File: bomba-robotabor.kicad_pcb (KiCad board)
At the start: 2 copper layers, 93 parts, among them U1 74HC03, U2 74HCT08, U3 L4904

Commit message: sfd,j
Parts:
- removed the REF** at (138.4, 59.7)
- removed the REF** at (194.3, 78.7)
- removed the REF** at (191.8, 76.2)
- removed the REF** at (194.3, 76.2)
- removed the REF** at (191.8, 73.7)
- removed the REF** at (194.3, 73.7)
- removed the REF** at (191.8, 71.1)
- removed the REF** at (194.3, 71.1)
- removed the REF** at (191.8, 68.6)
- removed the REF** at (194.3, 68.6)
- removed the REF** at (191.8, 66.0)
- removed the REF** at (138.4, 57.1)
- removed the REF** at (194.3, 66.0)
- removed the REF** at (191.8, 63.5)
- removed the REF** at (194.3, 63.5)
- removed the REF** at (191.8, 61.0)
- removed the REF** at (194.3, 61.0)
- removed the REF** at (191.8, 58.4)
- removed the REF** at (194.3, 58.4)
- removed the REF** at (191.8, 55.9)
- removed the REF** at (194.3, 55.9)
- removed the REF** at (191.8, 53.3)
- removed the REF** at (163.8, 67.3)
- removed the REF** at (194.3, 53.3)
- removed the REF** at (191.8, 50.8)
- removed the REF** at (194.3, 50.8)
- removed the REF** at (191.8, 48.3)
- removed the REF** at (194.3, 48.3)
- removed the REF** at (181.6, 61.0)
- removed the REF** at (181.6, 57.1)
- removed the REF** at (166.4, 61.0)
- removed the REF** at (166.4, 57.1)
- removed the REF** at (181.6, 77.5)
- removed the REF** at (163.8, 64.8)
- removed the REF** at (166.4, 77.5)
- removed the REF** at (156.2, 77.5)
- removed the REF** at (141.0, 77.5)
- removed the REF** at (130.8, 77.5)
- removed the REF** at (115.6, 77.5)
- removed the REF** at (179.1, 72.4)
- removed the REF** at (179.1, 69.8)
- removed the REF** at (179.1, 67.3)
- removed the REF** at (179.1, 64.8)
- removed the REF** at (166.4, 69.8)
- removed the REF** at (191.8, 83.8)
- removed the REF** at (166.4, 67.3)
- removed the REF** at (166.4, 64.8)
- removed the REF** at (153.7, 57.1)
- removed the REF** at (153.7, 59.7)
- removed the REF** at (153.7, 62.2)
- removed the REF** at (153.7, 64.8)
- removed the REF** at (153.7, 67.3)
- removed the REF** at (153.7, 69.8)
- removed the REF** at (141.0, 72.4)
- removed the REF** at (141.0, 69.8)
- removed the REF** at (194.3, 83.8)
- removed the REF** at (141.0, 67.3)
- removed the REF** at (141.0, 64.8)
- removed the REF** at (141.0, 62.2)
- removed the REF** at (141.0, 59.7)
- removed the REF** at (141.0, 57.1)
- removed the REF** at (167.6, 52.1)
- removed the REF** at (152.4, 52.1)
- removed the REF** at (129.5, 57.1)
- removed the REF** at (129.5, 59.7)
- removed the REF** at (129.5, 64.8)
- removed the REF** at (191.8, 81.3)
- removed the REF** at (116.8, 69.8)
- removed the REF** at (162.6, 82.5)
- removed the REF** at (160.0, 82.5)
- removed the REF** at (157.5, 82.5)
- removed the REF** at (162.6, 48.3)
- removed the REF** at (160.0, 48.3)
- removed the REF** at (166.4, 72.4)
- removed the REF** at (153.7, 72.4)
- removed the REF** at (129.5, 72.4)
- removed the REF** at (116.8, 72.4)
- removed the REF** at (194.3, 81.3)
- removed the REF** at (116.8, 59.7)
- removed the REF** at (116.8, 57.1)
- removed the REF** at (137.2, 52.1)
- removed the REF** at (121.9, 52.1)
- removed the REF** at (191.8, 78.7)
- added REF**: PinSocket_1x01_P2.54mm_Vertical, Connector_PinSocket_2.54mm:PinSocket_1x01_P2.54mm_Vertical, F.Cu at (156.2, 77.5)
- added REF**: PinSocket_1x01_P2.54mm_Vertical, Connector_PinSocket_2.54mm:PinSocket_1x01_P2.54mm_Vertical, F.Cu at (162.6, 82.5)
- added REF**: PinSocket_1x01_P2.54mm_Vertical, Connector_PinSocket_2.54mm:PinSocket_1x01_P2.54mm_Vertical, F.Cu at (160.0, 82.5)
- added REF**: PinSocket_1x01_P2.54mm_Vertical, Connector_PinSocket_2.54mm:PinSocket_1x01_P2.54mm_Vertical, F.Cu at (157.5, 82.5)
- added REF**: PinSocket_1x01_P2.54mm_Vertical, Connector_PinSocket_2.54mm:PinSocket_1x01_P2.54mm_Vertical, F.Cu at (141.0, 77.5)
- added REF**: PinSocket_1x01_P2.54mm_Vertical, Connector_PinSocket_2.54mm:PinSocket_1x01_P2.54mm_Vertical, F.Cu at (138.4, 59.7)
- added REF**: PinSocket_1x01_P2.54mm_Vertical, Connector_PinSocket_2.54mm:PinSocket_1x01_P2.54mm_Vertical, F.Cu at (138.4, 57.1)
- added REF**: PinSocket_1x01_P2.54mm_Vertical, Connector_PinSocket_2.54mm:PinSocket_1x01_P2.54mm_Vertical, F.Cu at (129.5, 57.1)
- added REF**: PinSocket_1x01_P2.54mm_Vertical, Connector_PinSocket_2.54mm:PinSocket_1x01_P2.54mm_Vertical, F.Cu at (129.5, 59.7)
- added REF**: PinSocket_1x01_P2.54mm_Vertical, Connector_PinSocket_2.54mm:PinSocket_1x01_P2.54mm_Vertical, F.Cu at (129.5, 64.8)
- added REF**: PinSocket_1x01_P2.54mm_Vertical, Connector_PinSocket_2.54mm:PinSocket_1x01_P2.54mm_Vertical, F.Cu at (129.5, 72.4)
- added REF**: PinSocket_1x01_P2.54mm_Vertical, Connector_PinSocket_2.54mm:PinSocket_1x01_P2.54mm_Vertical, F.Cu at (181.6, 61.0)
- added REF**: PinSocket_1x01_P2.54mm_Vertical, Connector_PinSocket_2.54mm:PinSocket_1x01_P2.54mm_Vertical, F.Cu at (130.8, 77.5)
- added REF**: PinSocket_1x01_P2.54mm_Vertical, Connector_PinSocket_2.54mm:PinSocket_1x01_P2.54mm_Vertical, F.Cu at (115.6, 77.5)
- added REF**: PinSocket_1x01_P2.54mm_Vertical, Connector_PinSocket_2.54mm:PinSocket_1x01_P2.54mm_Vertical, F.Cu at (116.8, 72.4)
- added REF**: PinSocket_1x01_P2.54mm_Vertical, Connector_PinSocket_2.54mm:PinSocket_1x01_P2.54mm_Vertical, F.Cu at (116.8, 69.8)
- added REF**: PinSocket_1x01_P2.54mm_Vertical, Connector_PinSocket_2.54mm:PinSocket_1x01_P2.54mm_Vertical, F.Cu at (116.8, 59.7)
- added REF**: PinSocket_1x01_P2.54mm_Vertical, Connector_PinSocket_2.54mm:PinSocket_1x01_P2.54mm_Vertical, F.Cu at (116.8, 57.1)
- added REF**: PinSocket_1x01_P2.54mm_Vertical, Connector_PinSocket_2.54mm:PinSocket_1x01_P2.54mm_Vertical, F.Cu at (137.2, 52.1)
- added REF**: PinSocket_1x01_P2.54mm_Vertical, Connector_PinSocket_2.54mm:PinSocket_1x01_P2.54mm_Vertical, F.Cu at (121.9, 52.1)
- added REF**: PinSocket_1x01_P2.54mm_Vertical, Connector_PinSocket_2.54mm:PinSocket_1x01_P2.54mm_Vertical, F.Cu at (162.6, 48.3)
- added REF**: PinSocket_1x01_P2.54mm_Vertical, Connector_PinSocket_2.54mm:PinSocket_1x01_P2.54mm_Vertical, F.Cu at (160.0, 48.3)
- added REF**: PinSocket_1x01_P2.54mm_Vertical, Connector_PinSocket_2.54mm:PinSocket_1x01_P2.54mm_Vertical, F.Cu at (181.6, 57.1)
- added REF**: PinSocket_1x01_P2.54mm_Vertical, Connector_PinSocket_2.54mm:PinSocket_1x01_P2.54mm_Vertical, F.Cu at (152.4, 52.1)
- added REF**: PinSocket_1x01_P2.54mm_Vertical, Connector_PinSocket_2.54mm:PinSocket_1x01_P2.54mm_Vertical, F.Cu at (167.6, 52.1)
- added REF**: PinSocket_1x04_P2.54mm_Vertical, Connector_PinSocket_2.54mm:PinSocket_1x04_P2.54mm_Vertical, F.Cu at (166.4, 64.8)
- added REF**: PinSocket_1x04_P2.54mm_Vertical, Connector_PinSocket_2.54mm:PinSocket_1x04_P2.54mm_Vertical, F.Cu at (179.1, 64.8)
- added REF**: PinSocket_1x07_P2.54mm_Vertical, Connector_PinSocket_2.54mm:PinSocket_1x07_P2.54mm_Vertical, F.Cu at (153.7, 57.1)
- added REF**: PinSocket_1x07_P2.54mm_Vertical, Connector_PinSocket_2.54mm:PinSocket_1x07_P2.54mm_Vertical, F.Cu at (141.0, 57.1)
- added REF**: PinHeader_2x15_P2.54mm_Vertical, Connector_PinHeader_2.54mm:PinHeader_2x15_P2.54mm_Vertical, F.Cu at (191.8, 48.3)
- added REF**: PinSocket_1x01_P2.54mm_Vertical, Connector_PinSocket_2.54mm:PinSocket_1x01_P2.54mm_Vertical, F.Cu at (166.4, 61.0)
- added REF**: PinSocket_1x01_P2.54mm_Vertical, Connector_PinSocket_2.54mm:PinSocket_1x01_P2.54mm_Vertical, F.Cu at (166.4, 57.1)
- added REF**: PinSocket_1x01_P2.54mm_Vertical, Connector_PinSocket_2.54mm:PinSocket_1x01_P2.54mm_Vertical, F.Cu at (163.8, 67.3)
- added REF**: PinSocket_1x01_P2.54mm_Vertical, Connector_PinSocket_2.54mm:PinSocket_1x01_P2.54mm_Vertical, F.Cu at (163.8, 64.8)
- added REF**: PinSocket_1x01_P2.54mm_Vertical, Connector_PinSocket_2.54mm:PinSocket_1x01_P2.54mm_Vertical, F.Cu at (181.6, 77.5)
- added REF**: PinSocket_1x01_P2.54mm_Vertical, Connector_PinSocket_2.54mm:PinSocket_1x01_P2.54mm_Vertical, F.Cu at (166.4, 77.5)

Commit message: pcb 2 layers
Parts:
- REF**: moved to B.Cu
- moved REF** 35.6 mm to (191.8, 83.8)
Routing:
- net (no net): track 346.9 -> 796.7 mm

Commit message: done?
not checked
not polished
just connected
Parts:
- removed the REF** at (181.6, 77.5)
- removed the REF** at (162.6, 82.5)
- removed the REF** at (160.0, 82.5)
- removed the REF** at (157.5, 82.5)
- removed the REF** at (141.0, 77.5)
- removed the REF** at (138.4, 59.7)
- removed the REF** at (138.4, 57.1)
- removed the REF** at (129.5, 57.1)
- removed the REF** at (129.5, 59.7)
- removed the REF** at (129.5, 64.8)
- removed the REF** at (129.5, 72.4)
- removed the REF** at (156.2, 77.5)
- removed the REF** at (130.8, 77.5)
- removed the REF** at (115.6, 77.5)
- removed the REF** at (116.8, 72.4)
- removed the REF** at (116.8, 69.8)
- removed the REF** at (116.8, 59.7)
- removed the REF** at (116.8, 57.1)
- removed the REF** at (137.2, 52.1)
- removed the REF** at (121.9, 52.1)
- removed the REF** at (162.6, 48.3)
- removed the REF** at (160.0, 48.3)
- removed the REF** at (181.6, 61.0)
- removed the REF** at (152.4, 52.1)
- removed the REF** at (167.6, 52.1)
- removed the REF** at (179.1, 64.8)
- removed the REF** at (181.6, 57.1)
- removed the REF** at (166.4, 61.0)
- removed the REF** at (166.4, 57.1)
- removed the REF** at (163.8, 67.3)
- removed the REF** at (163.8, 64.8)
- removed the REF** at (166.4, 77.5)
- added  : PinSocket_1x01_P2.54mm_Vertical, Connector_PinSocket_2.54mm:PinSocket_1x01_P2.54mm_Vertical, F.Cu at (166.4, 77.5)
- added  : PinSocket_1x01_P2.54mm_Vertical, Connector_PinSocket_2.54mm:PinSocket_1x01_P2.54mm_Vertical, F.Cu at (162.6, 82.5)
- added  : PinSocket_1x01_P2.54mm_Vertical, Connector_PinSocket_2.54mm:PinSocket_1x01_P2.54mm_Vertical, F.Cu at (160.0, 82.5)
- added  : PinSocket_1x01_P2.54mm_Vertical, Connector_PinSocket_2.54mm:PinSocket_1x01_P2.54mm_Vertical, F.Cu at (157.5, 82.5)
- added  : PinSocket_1x01_P2.54mm_Vertical, Connector_PinSocket_2.54mm:PinSocket_1x01_P2.54mm_Vertical, F.Cu at (141.0, 77.5)
- added  : PinSocket_1x01_P2.54mm_Vertical, Connector_PinSocket_2.54mm:PinSocket_1x01_P2.54mm_Vertical, F.Cu at (138.4, 59.7)
- added  : PinSocket_1x01_P2.54mm_Vertical, Connector_PinSocket_2.54mm:PinSocket_1x01_P2.54mm_Vertical, F.Cu at (138.4, 57.1)
- added  : PinSocket_1x01_P2.54mm_Vertical, Connector_PinSocket_2.54mm:PinSocket_1x01_P2.54mm_Vertical, F.Cu at (129.5, 57.1)
- added  : PinSocket_1x01_P2.54mm_Vertical, Connector_PinSocket_2.54mm:PinSocket_1x01_P2.54mm_Vertical, F.Cu at (129.5, 59.7)
- added  : PinSocket_1x01_P2.54mm_Vertical, Connector_PinSocket_2.54mm:PinSocket_1x01_P2.54mm_Vertical, F.Cu at (129.5, 64.8)
- added  : PinSocket_1x01_P2.54mm_Vertical, Connector_PinSocket_2.54mm:PinSocket_1x01_P2.54mm_Vertical, F.Cu at (181.6, 77.5)
- added  : PinSocket_1x01_P2.54mm_Vertical, Connector_PinSocket_2.54mm:PinSocket_1x01_P2.54mm_Vertical, F.Cu at (129.5, 72.4)
- added  : PinSocket_1x01_P2.54mm_Vertical, Connector_PinSocket_2.54mm:PinSocket_1x01_P2.54mm_Vertical, F.Cu at (130.8, 77.5)
- added  : PinSocket_1x01_P2.54mm_Vertical, Connector_PinSocket_2.54mm:PinSocket_1x01_P2.54mm_Vertical, F.Cu at (115.6, 77.5)
- added  : PinSocket_1x01_P2.54mm_Vertical, Connector_PinSocket_2.54mm:PinSocket_1x01_P2.54mm_Vertical, F.Cu at (116.8, 72.4)
- added  : PinSocket_1x01_P2.54mm_Vertical, Connector_PinSocket_2.54mm:PinSocket_1x01_P2.54mm_Vertical, F.Cu at (116.8, 69.8)
- added  : PinSocket_1x01_P2.54mm_Vertical, Connector_PinSocket_2.54mm:PinSocket_1x01_P2.54mm_Vertical, F.Cu at (116.8, 59.7)
- added  : PinSocket_1x01_P2.54mm_Vertical, Connector_PinSocket_2.54mm:PinSocket_1x01_P2.54mm_Vertical, F.Cu at (116.8, 57.1)
- added  : PinSocket_1x01_P2.54mm_Vertical, Connector_PinSocket_2.54mm:PinSocket_1x01_P2.54mm_Vertical, F.Cu at (137.2, 52.1)
- added  : PinSocket_1x01_P2.54mm_Vertical, Connector_PinSocket_2.54mm:PinSocket_1x01_P2.54mm_Vertical, F.Cu at (121.9, 52.1)
- added  : PinSocket_1x01_P2.54mm_Vertical, Connector_PinSocket_2.54mm:PinSocket_1x01_P2.54mm_Vertical, F.Cu at (162.6, 48.3)
- added  : PinSocket_1x01_P2.54mm_Vertical, Connector_PinSocket_2.54mm:PinSocket_1x01_P2.54mm_Vertical, F.Cu at (156.2, 77.5)
- added  : PinSocket_1x01_P2.54mm_Vertical, Connector_PinSocket_2.54mm:PinSocket_1x01_P2.54mm_Vertical, F.Cu at (160.0, 48.3)
- added  : PinSocket_1x01_P2.54mm_Vertical, Connector_PinSocket_2.54mm:PinSocket_1x01_P2.54mm_Vertical, F.Cu at (152.4, 52.1)
- added  : PinSocket_1x01_P2.54mm_Vertical, Connector_PinSocket_2.54mm:PinSocket_1x01_P2.54mm_Vertical, F.Cu at (167.6, 52.1)
- added  : PinSocket_1x01_P2.54mm_Vertical, Connector_PinSocket_2.54mm:PinSocket_1x01_P2.54mm_Vertical, F.Cu at (181.6, 61.0)
- added  : PinSocket_1x01_P2.54mm_Vertical, Connector_PinSocket_2.54mm:PinSocket_1x01_P2.54mm_Vertical, F.Cu at (181.6, 57.1)
- added  : PinSocket_1x01_P2.54mm_Vertical, Connector_PinSocket_2.54mm:PinSocket_1x01_P2.54mm_Vertical, F.Cu at (166.4, 61.0)
- added  : PinSocket_1x01_P2.54mm_Vertical, Connector_PinSocket_2.54mm:PinSocket_1x01_P2.54mm_Vertical, F.Cu at (166.4, 57.1)
- added  : PinSocket_1x01_P2.54mm_Vertical, Connector_PinSocket_2.54mm:PinSocket_1x01_P2.54mm_Vertical, F.Cu at (163.8, 67.3)
- added  : PinSocket_1x01_P2.54mm_Vertical, Connector_PinSocket_2.54mm:PinSocket_1x01_P2.54mm_Vertical, F.Cu at (163.8, 64.8)
- added REF**: PinSocket_1x03_P2.54mm_Vertical, Connector_PinSocket_2.54mm:PinSocket_1x03_P2.54mm_Vertical, F.Cu at (179.1, 64.8)
-  : renamed from REF** (x3)
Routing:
- net (no net): track 796.7 -> 1446.5 mm

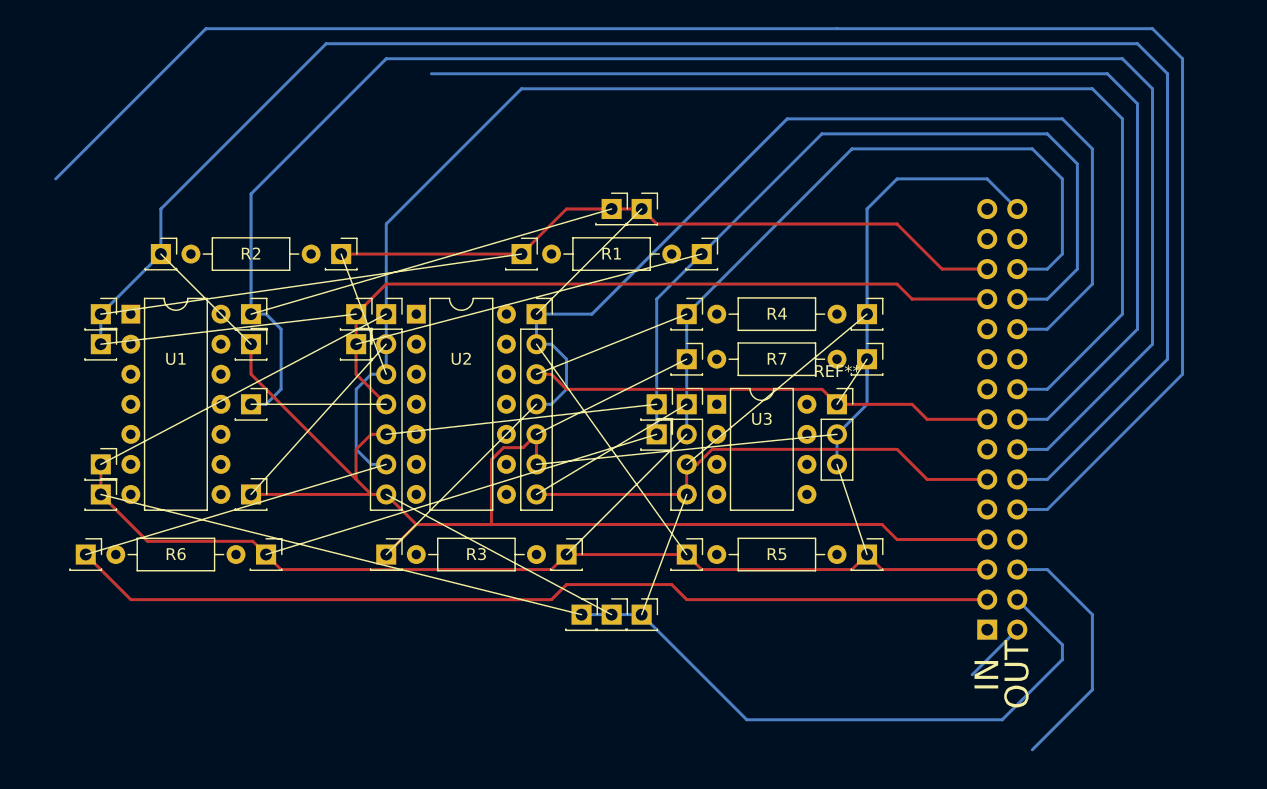
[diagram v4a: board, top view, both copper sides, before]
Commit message: tidying up + LED + piezo + RESET button
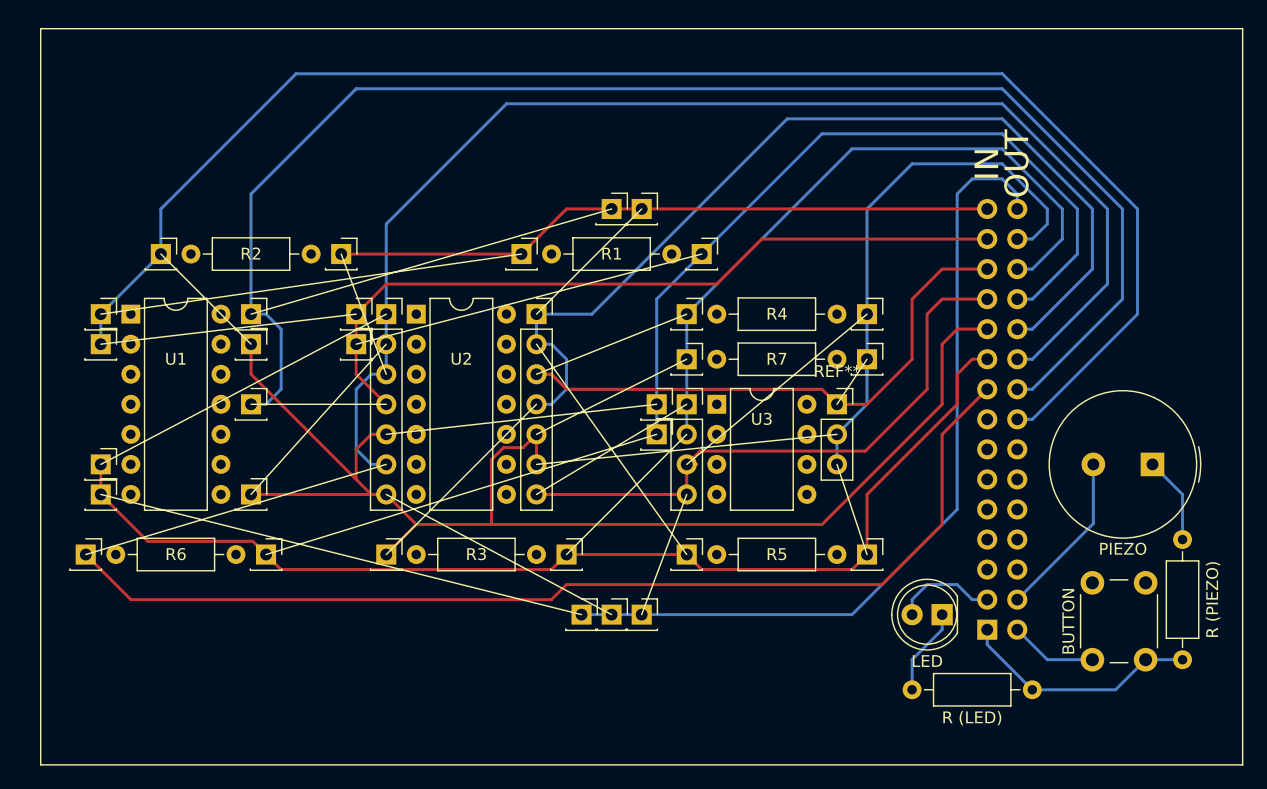
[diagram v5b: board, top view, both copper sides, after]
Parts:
- added BUTTON: SW_PUSH_6mm_H8.5mm, Button_Switch_THT:SW_PUSH_6mm_H8.5mm, F.Cu at (200.7, 86.4)
- added LED: LED_D5.0mm, LED_THT:LED_D5.0mm, F.Cu at (188.0, 82.5)
- added PIEZO: Buzzer_TDK_PS1240P02BT_D12.2mm_H6.5mm, Buzzer_Beeper:Buzzer_TDK_PS1240P02BT_D12.2mm_H6.5mm, F.Cu at (205.7, 69.8)
- added R (LED): R_Axial_DIN0207_L6.3mm_D2.5mm_P10.16mm_Horizontal, Resistor_THT:R_Axial_DIN0207_L6.3mm_D2.5mm_P10.16mm_Horizontal, F.Cu at (195.6, 88.9)
- added R (PIEZO): R_Axial_DIN0207_L6.3mm_D2.5mm_P10.16mm_Horizontal, Resistor_THT:R_Axial_DIN0207_L6.3mm_D2.5mm_P10.16mm_Horizontal, F.Cu at (208.3, 86.4)
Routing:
- net (no net): track 1446.4 -> 1259.8 mm

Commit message: *design*
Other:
- board text added: "BOMB BASIC"
- board text added: "by phuid & milda"
- board text added: "if something is wrong blame phuid"

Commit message: BASIC + +- on polar
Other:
- board text added: "+"
- board text added: "-"
- board text added: "BASIC"
- board text added: "by phuid & Midla"
- board text removed: "by phuid & milda"
